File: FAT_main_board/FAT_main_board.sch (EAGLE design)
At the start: 19 parts, among them IC1 74LS241N

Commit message: [FAT board] Adds UART and I2C connectors.
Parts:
- added I2C0, I2C1, I2C2, UART1, UART2, UART3, UART4: (no value), con-lstb:MA04-1
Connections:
- removed net N$13: U$1.GND
- removed net RX0: U$1.0/RX
- removed net TX0: U$1.1/TX
- new net RX1: U$1.0/RX, UART1.1
- new net TX1: U$1.1/TX, UART1.2
- net GND: now also I2C0.3, I2C1.3, I2C2.3, U$1.GND, UART1.3, UART2.3, UART3.3, UART4.3
- net RX2: now also UART2.1
- net RX3: now also UART3.1
- net RX4: now also UART4.1
- net SCL0: now also I2C0.1
- net SCL1: now also I2C1.1
- net SCL2: now also I2C2.1
- net SDA0: now also I2C0.2
- net SDA1: now also I2C1.2
- net SDA2: now also I2C2.2
- net TX2: now also UART2.2
- net TX3: now also UART3.2
- net TX4: now also UART4.2
- net VCC: now also I2C0.4, I2C1.4, I2C2.4, U$1.VIN, UART1.4, UART2.4, UART3.4, UART4.4
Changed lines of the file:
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@@
 <part name="R4" library="resistor" deviceset="R-EU_" device="0204/7" value="10K"/>
 <part name="SV1" library="con-lstb" deviceset="MA03-1" device=""/>
+<part name="UART1" library="con-lstb" deviceset="MA04-1" device=""/>
+<part name="UART2" library="con-lstb" deviceset="MA04-1" device=""/>
+<part name="I2C0" library="con-lstb" deviceset="MA04-1" device=""/>
+<part name="I2C1" library="con-lstb" deviceset="MA04-1" device=""/>
+<part name="UART3" library="con-lstb" deviceset="MA04-1" device=""/>
+<part name="UART4" library="con-lstb" deviceset="MA04-1" device=""/>
+<part name="I2C2" library="con-lstb" deviceset="MA04-1" device=""/>
 </parts>
 <sheets>
@@
 <instance part="R4" gate="G$1" x="119.38" y="-99.06" rot="R90"/>
 <instance part="SV1" gate="G$1" x="213.36" y="-116.84" rot="R180"/>
+<instance part="UART1" gate="1" x="-111.76" y="25.4"/>
+<instance part="UART2" gate="1" x="-111.76" y="7.62"/>
+<instance part="I2C0" gate="1" x="-142.24" y="25.4"/>
+<instance part="I2C1" gate="1" x="-142.24" y="7.62"/>
+<instance part="UART3" gate="1" x="-111.76" y="-12.7"/>
+<instance part="UART4" gate="1" x="-111.76" y="-33.02"/>
+<instance part="I2C2" gate="1" x="-142.24" y="-12.7"/>
 </instances>
 <busses>
@@
 <label x="185.42" y="-114.3" size="1.778" layer="95"/>
 </segment>
+<segment>
+<pinref part="U$1" gate="G$1" pin="GND"/>
+<wire x1="-20.32" y1="22.86" x2="-27.94" y2="22.86" width="0.1524" layer="91"/>
+<label x="-27.94" y="22.86" size="1.778" layer="95"/>
+</segment>
+<segment>
+<pinref part="UART1" gate="1" pin="3"/>
+<wire x1="-104.14" y1="25.4" x2="-93.98" y2="25.4" width="0.1524" layer="91"/>
+<label x="-99.06" y="25.4" size="1.778" layer="95"/>
+</segment>
+<segment>
+<pinref part="UART2" gate="1" pin="3"/>
+<wire x1="-93.98" y1="7.62" x2="-104.14" y2="7.62" width="0.1524" layer="91"/>
+<label x="-99.06" y="7.62" size="1.778" layer="95"/>
+</segment>
+<segment>
+<pinref part="UART3" gate="1" pin="3"/>
+<wire x1="-93.98" y1="-12.7" x2="-104.14" y2="-12.7" width="0.1524" layer="91"/>
+<label x="-99.06" y="-12.7" size="1.778" layer="95"/>
+</segment>
+<segment>
+<pinref part="UART4" gate="1" pin="3"/>
+<wire x1="-93.98" y1="-33.02" x2="-104.14" y2="-33.02" width="0.1524" layer="91"/>
+<label x="-99.06" y="-33.02" size="1.778" layer="95"/>
+</segment>
+<segment>
+<pinref part="I2C0" gate="1" pin="3"/>
+<wire x1="-134.62" y1="25.4" x2="-124.46" y2="25.4" width="0.1524" layer="91"/>
+<label x="-129.54" y="25.4" size="1.778" layer="95"/>
+</segment>
+<segment>
+<pinref part="I2C1" gate="1" pin="3"/>
+<wire x1="-134.62" y1="7.62" x2="-124.46" y2="7.62" width="0.1524" layer="91"/>
+<label x="-129.54" y="7.62" size="1.778" layer="95"/>
+</segment>
+<segment>
+<pinref part="I2C2" gate="1" pin="3"/>
+<wire x1="-134.62" y1="-12.7" x2="-124.46" y2="-12.7" width="0.1524" layer="91"/>
+<label x="-129.54" y="-12.7" size="1.778" layer="95"/>
+</segment>
 </net>
 <net name="VCC" class="0">
@@
 <wire x1="109.22" y1="-124.46" x2="99.06" y2="-124.46" width="0.1524" layer="91"/>
 <label x="99.06" y="-124.46" size="1.778" layer="95"/>
+</segment>
+<segment>
+<pinref part="U$1" gate="G$1" pin="VIN"/>
+<wire x1="20.32" y1="22.86" x2="30.48" y2="22.86" width="0.1524" layer="91"/>
+<label x="25.4" y="22.86" size="1.778" layer="95"/>
+</segment>
+<segment>
+<pinref part="UART1" gate="1" pin="4"/>
+<wire x1="-104.14" y1="27.94" x2="-93.98" y2="27.94" width="0.1524" layer="91"/>
+<label x="-99.06" y="27.94" size="1.778" layer="95"/>
+</segment>
+<segment>
+<pinref part="UART2" gate="1" pin="4"/>
+<wire x1="-104.14" y1="10.16" x2="-93.98" y2="10.16" width="0.1524" layer="91"/>
+<label x="-99.06" y="10.16" size="1.778" layer="95"/>
+</segment>
+<segment>
+<pinref part="UART3" gate="1" pin="4"/>
+<wire x1="-104.14" y1="-10.16" x2="-93.98" y2="-10.16" width="0.1524" layer="91"/>
+<label x="-99.06" y="-10.16" size="1.778" layer="95"/>
+</segment>
+<segment>
+<pinref part="UART4" gate="1" pin="4"/>
+<wire x1="-104.14" y1="-30.48" x2="-93.98" y2="-30.48" width="0.1524" layer="91"/>
+<label x="-99.06" y="-30.48" size="1.778" layer="95"/>
+</segment>
+<segment>
+<pinref part="I2C0" gate="1" pin="4"/>
+<wire x1="-124.46" y1="27.94" x2="-134.62" y2="27.94" width="0.1524" layer="91"/>
+<label x="-129.54" y="27.94" size="1.778" layer="95"/>
+</segment>
+<segment>
+<pinref part="I2C1" gate="1" pin="4"/>
+<wire x1="-124.46" y1="10.16" x2="-134.62" y2="10.16" width="0.1524" layer="91"/>
+<label x="-129.54" y="10.16" size="1.778" layer="95"/>
+</segment>
+<segment>
+<pinref part="I2C2" gate="1" pin="4"/>
+<wire x1="-124.46" y1="-10.16" x2="-134.62" y2="-10.16" width="0.1524" layer="91"/>
+<label x="-129.54" y="-10.16" size="1.778" layer="95"/>
 </segment>
 </net>
@@
 <label x="25.4" y="5.08" size="1.778" layer="95"/>
 </segment>
+<segment>
+<pinref part="I2C0" gate="1" pin="1"/>
+<wire x1="-134.62" y1="20.32" x2="-124.46" y2="20.32" width="0.1524" layer="91"/>
+<label x="-129.54" y="20.32" size="1.778" layer="95"/>
+</segment>
 </net>
 <net name="SDA0" class="0">
@@
 <label x="25.4" y="2.54" size="1.778" layer="95"/>
 </segment>
+<segment>
+<pinref part="I2C0" gate="1" pin="2"/>
+<wire x1="-124.46" y1="22.86" x2="-134.62" y2="22.86" width="0.1524" layer="91"/>
+<label x="-129.54" y="22.86" size="1.778" layer="95"/>
+</segment>
 </net>
 <net name="SDA1" class="0">
@@
 <label x="25.4" y="-22.86" size="1.778" layer="95"/>
 </segment>
+<segment>
+<pinref part="I2C1" gate="1" pin="2"/>
+<wire x1="-124.46" y1="5.08" x2="-134.62" y2="5.08" width="0.1524" layer="91"/>
+<label x="-129.54" y="5.08" size="1.778" layer="95"/>
+</segment>
 </net>
 <net name="SCL1" class="0">
@@
 <label x="25.4" y="-25.4" size="1.778" layer="95"/>
 </segment>
+<segment>
+<pinref part="I2C1" gate="1" pin="1"/>
+<wire x1="-134.62" y1="2.54" x2="-124.46" y2="2.54" width="0.1524" layer="91"/>
+<label x="-129.54" y="2.54" size="1.778" layer="95"/>
+</segment>
 </net>
 <net name="RX5" class="0">
@@
 <label x="-30.48" y="-35.56" size="1.778" layer="95"/>
 </segment>
+<segment>
+<pinref part="UART4" gate="1" pin="2"/>
+<wire x1="-104.14" y1="-35.56" x2="-93.98" y2="-35.56" width="0.1524" layer="91"/>
+<label x="-99.06" y="-35.56" size="1.778" layer="95"/>
+</segment>
 </net>
 <net name="RX4" class="0">
@@
 <label x="-30.48" y="-33.02" size="1.778" layer="95"/>
 </segment>
+<segment>
+<pinref part="UART4" gate="1" pin="1"/>
+<wire x1="-93.98" y1="-38.1" x2="-104.14" y2="-38.1" width="0.1524" layer="91"/>
+<label x="-99.06" y="-38.1" size="1.778" layer="95"/>
+</segment>
 </net>
 <net name="N$40" class="0">
@@
 <label x="-30.48" y="-5.08" size="1.778" layer="95"/>
 </segment>
+<segment>
+<pinref part="UART2" gate="1" pin="2"/>
+<wire x1="-104.14" y1="5.08" x2="-93.98" y2="5.08" width="0.1524" layer="91"/>
+<label x="-99.06" y="5.08" size="1.778" layer="95"/>
+</segment>
 </net>
 <net name="RX2" class="0">
@@
 <label x="-30.48" y="-2.54" size="1.778" layer="95"/>
 </segment>
+<segment>
+<pinref part="UART2" gate="1" pin="1"/>
+<wire x1="-93.98" y1="2.54" x2="-104.14" y2="2.54" width="0.1524" layer="91"/>
+<label x="-99.06" y="2.54" size="1.778" layer="95"/>
+</segment>
 </net>
 <net name="TX3" class="0">
@@
 <label x="-30.48" y="0" size="1.778" layer="95"/>
 </segment>
+<segment>
+<pinref part="UART3" gate="1" pin="2"/>
+<wire x1="-104.14" y1="-15.24" x2="-93.98" y2="-15.24" width="0.1524" layer="91"/>
+<label x="-99.06" y="-15.24" size="1.778" layer="95"/>
+</segment>
 </net>
 <net name="RX3" class="0">
@@
 <label x="-30.48" y="2.54" size="1.778" layer="95"/>
 </segment>
-</net>
-<net name="RX0" class="0">
+<segment>
+<pinref part="UART3" gate="1" pin="1"/>
+<wire x1="-93.98" y1="-17.78" x2="-104.14" y2="-17.78" width="0.1524" layer="91"/>
+<label x="-99.06" y="-17.78" size="1.778" layer="95"/>
+</segment>
+</net>
+<net name="RX1" class="0">
 <segment>
 <pinref part="U$1" gate="G$1" pin="0/RX"/>
@@
 <label x="-30.48" y="20.32" size="1.778" layer="95"/>
 </segment>
-</net>
-<net name="TX0" class="0">
+<segment>
+<pinref part="UART1" gate="1" pin="1"/>
+<wire x1="-104.14" y1="20.32" x2="-93.98" y2="20.32" width="0.1524" layer="91"/>
+<label x="-99.06" y="20.32" size="1.778" layer="95"/>
+</segment>
+</net>
+<net name="TX1" class="0">
 <segment>
 <pinref part="U$1" gate="G$1" pin="1/TX"/>
@@
 <label x="-30.48" y="17.78" size="1.778" layer="95"/>
 </segment>
+<segment>
+<pinref part="UART1" gate="1" pin="2"/>
+<wire x1="-93.98" y1="22.86" x2="-104.14" y2="22.86" width="0.1524" layer="91"/>
+<label x="-99.06" y="22.86" size="1.778" layer="95"/>
+</segment>
 </net>
 <net name="SCL2" class="0">
@@
 <label x="-30.48" y="12.7" size="1.778" layer="95"/>
 </segment>
+<segment>
+<pinref part="I2C2" gate="1" pin="1"/>
+<wire x1="-134.62" y1="-17.78" x2="-124.46" y2="-17.78" width="0.1524" layer="91"/>
+<label x="-129.54" y="-17.78" size="1.778" layer="95"/>
+</segment>
 </net>
 <net name="SDA2" class="0">
@@
 <label x="-30.48" y="10.16" size="1.778" layer="95"/>
 </segment>
+<segment>
+<pinref part="I2C2" gate="1" pin="2"/>
+<wire x1="-124.46" y1="-15.24" x2="-134.62" y2="-15.24" width="0.1524" layer="91"/>
+<label x="-129.54" y="-15.24" size="1.778" layer="95"/>
+</segment>
 </net>
 <net name="N$9" class="0">
@@
 </segment>
 </net>
-<net name="N$13" class="0">
-<segment>
-<pinref part="U$1" gate="G$1" pin="GND"/>
-<wire x1="-20.32" y1="22.86" x2="-27.94" y2="22.86" width="0.1524" layer="91"/>
-</segment>
-</net>

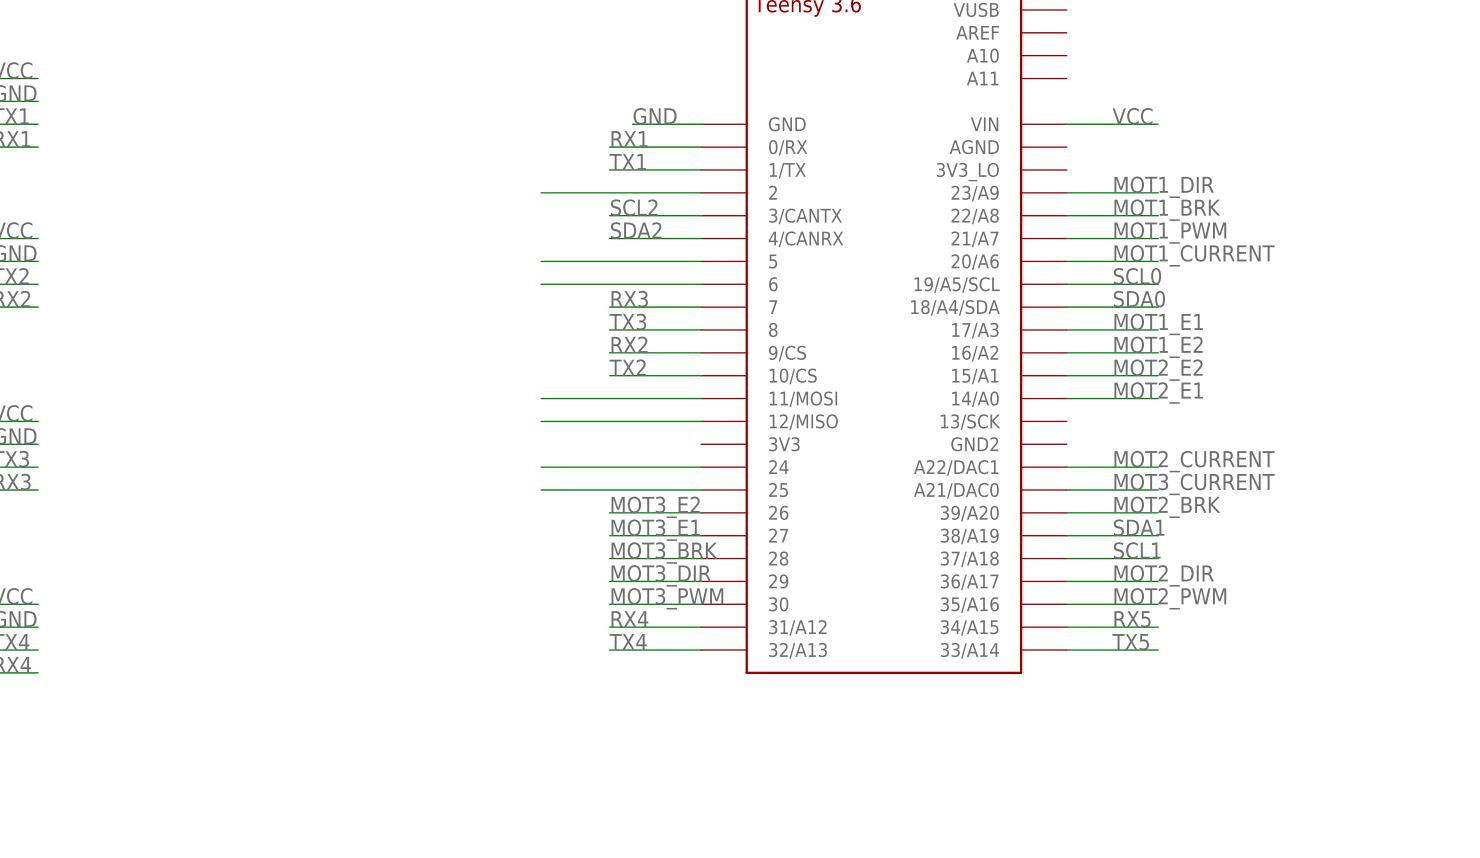
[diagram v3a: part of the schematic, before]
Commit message: [FAT board] Adds connector for free pins.
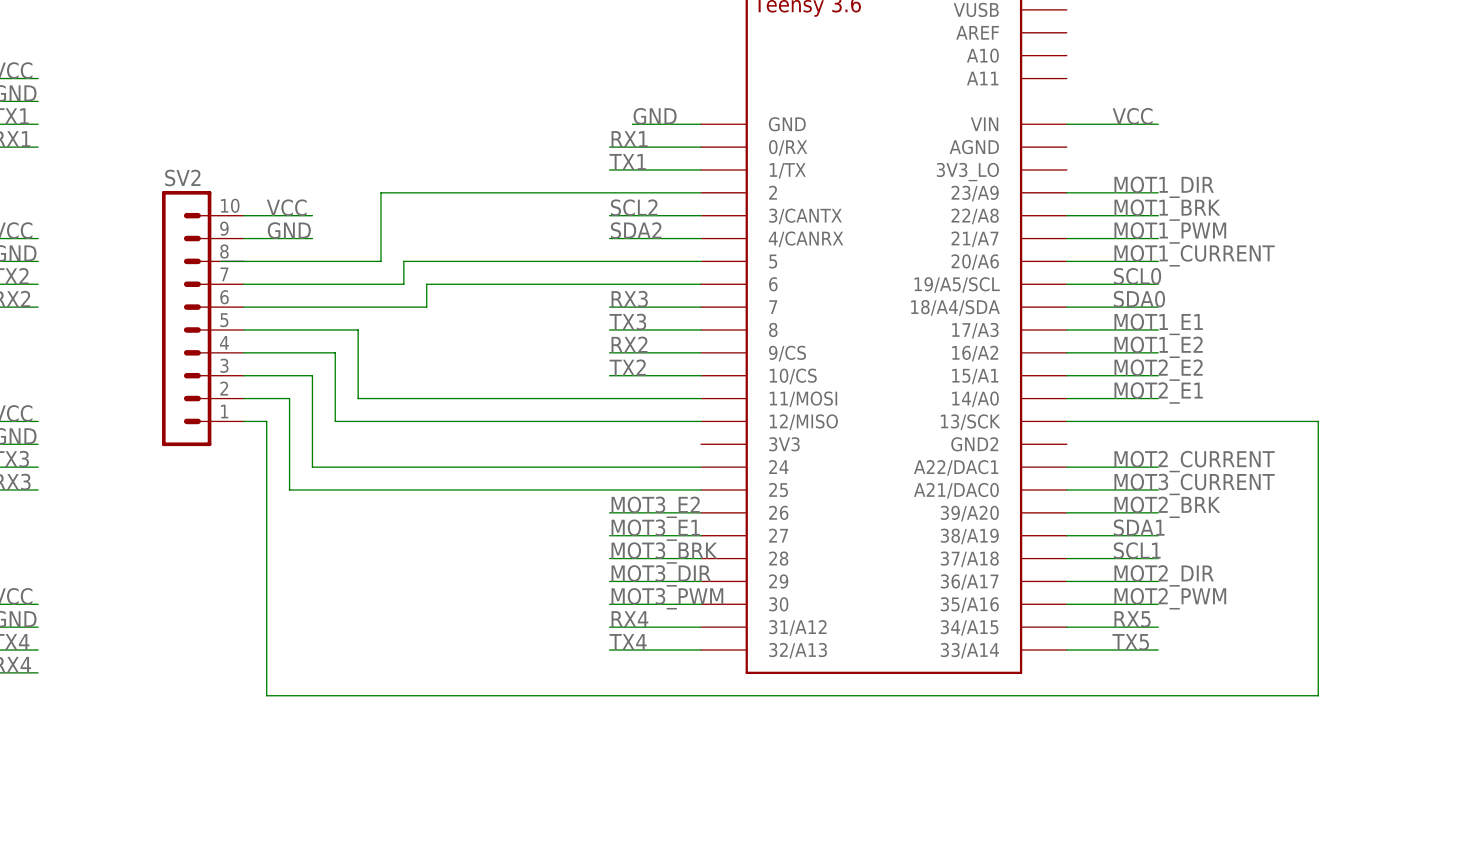
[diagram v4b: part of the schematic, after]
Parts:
- added SV2: (no value), con-lstb:MA10-1
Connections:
- new net N$24: SV2.1, U$1.13/SCK
- net GND: now also SV2.9
- net N$10: now also SV2.6
- net N$11: now also SV2.5
- net N$12: now also SV2.4
- net N$40: now also SV2.2
- net N$41: now also SV2.3
- net N$9: now also SV2.7
- net VCC: now also SV2.10
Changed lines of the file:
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@@
 <part name="UART4" library="con-lstb" deviceset="MA04-1" device=""/>
 <part name="I2C2" library="con-lstb" deviceset="MA04-1" device=""/>
+<part name="SV2" library="con-lstb" deviceset="MA10-1" device=""/>
 </parts>
 <sheets>
@@
 <instance part="UART4" gate="1" x="-111.76" y="-33.02"/>
 <instance part="I2C2" gate="1" x="-142.24" y="-12.7"/>
+<instance part="SV2" gate="1" x="-78.74" y="0"/>
 </instances>
 <busses>
@@
 <label x="-129.54" y="-12.7" size="1.778" layer="95"/>
 </segment>
+<segment>
+<pinref part="SV2" gate="1" pin="9"/>
+<wire x1="-71.12" y1="10.16" x2="-63.5" y2="10.16" width="0.1524" layer="91"/>
+<label x="-68.58" y="10.16" size="1.778" layer="95"/>
+</segment>
 </net>
 <net name="VCC" class="0">
@@
 <wire x1="-124.46" y1="-10.16" x2="-134.62" y2="-10.16" width="0.1524" layer="91"/>
 <label x="-129.54" y="-10.16" size="1.778" layer="95"/>
+</segment>
+<segment>
+<pinref part="SV2" gate="1" pin="10"/>
+<wire x1="-71.12" y1="12.7" x2="-63.5" y2="12.7" width="0.1524" layer="91"/>
+<label x="-68.58" y="12.7" size="1.778" layer="95"/>
 </segment>
 </net>
@@
 <segment>
 <pinref part="U$1" gate="G$1" pin="25"/>
-<wire x1="-38.1" y1="-17.78" x2="-20.32" y2="-17.78" width="0.1524" layer="91"/>
+<pinref part="SV2" gate="1" pin="2"/>
+<wire x1="-71.12" y1="-7.62" x2="-66.04" y2="-7.62" width="0.1524" layer="91"/>
+<wire x1="-66.04" y1="-7.62" x2="-66.04" y2="-17.78" width="0.1524" layer="91"/>
+<wire x1="-66.04" y1="-17.78" x2="-20.32" y2="-17.78" width="0.1524" layer="91"/>
 </segment>
 </net>
@@
 <segment>
 <pinref part="U$1" gate="G$1" pin="24"/>
-<wire x1="-20.32" y1="-15.24" x2="-38.1" y2="-15.24" width="0.1524" layer="91"/>
+<pinref part="SV2" gate="1" pin="3"/>
+<wire x1="-71.12" y1="-5.08" x2="-63.5" y2="-5.08" width="0.1524" layer="91"/>
+<wire x1="-63.5" y1="-5.08" x2="-63.5" y2="-15.24" width="0.1524" layer="91"/>
+<wire x1="-63.5" y1="-15.24" x2="-20.32" y2="-15.24" width="0.1524" layer="91"/>
 </segment>
 </net>
@@
 <segment>
 <pinref part="U$1" gate="G$1" pin="5"/>
-<wire x1="-20.32" y1="7.62" x2="-38.1" y2="7.62" width="0.1524" layer="91"/>
+<wire x1="-20.32" y1="7.62" x2="-53.34" y2="7.62" width="0.1524" layer="91"/>
+<pinref part="SV2" gate="1" pin="7"/>
+<wire x1="-71.12" y1="5.08" x2="-53.34" y2="5.08" width="0.1524" layer="91"/>
+<wire x1="-53.34" y1="5.08" x2="-53.34" y2="7.62" width="0.1524" layer="91"/>
 </segment>
 </net>
@@
 <segment>
 <pinref part="U$1" gate="G$1" pin="6"/>
-<wire x1="-38.1" y1="5.08" x2="-20.32" y2="5.08" width="0.1524" layer="91"/>
+<wire x1="-50.8" y1="5.08" x2="-20.32" y2="5.08" width="0.1524" layer="91"/>
+<pinref part="SV2" gate="1" pin="6"/>
+<wire x1="-71.12" y1="2.54" x2="-50.8" y2="2.54" width="0.1524" layer="91"/>
+<wire x1="-50.8" y1="2.54" x2="-50.8" y2="5.08" width="0.1524" layer="91"/>
 </segment>
 </net>
@@
 <segment>
 <pinref part="U$1" gate="G$1" pin="11/MOSI"/>
-<wire x1="-20.32" y1="-7.62" x2="-38.1" y2="-7.62" width="0.1524" layer="91"/>
+<pinref part="SV2" gate="1" pin="5"/>
+<wire x1="-71.12" y1="0" x2="-58.42" y2="0" width="0.1524" layer="91"/>
+<wire x1="-58.42" y1="0" x2="-58.42" y2="-7.62" width="0.1524" layer="91"/>
+<wire x1="-58.42" y1="-7.62" x2="-20.32" y2="-7.62" width="0.1524" layer="91"/>
 </segment>
 </net>
@@
 <segment>
 <pinref part="U$1" gate="G$1" pin="12/MISO"/>
-<wire x1="-38.1" y1="-10.16" x2="-20.32" y2="-10.16" width="0.1524" layer="91"/>
+<pinref part="SV2" gate="1" pin="4"/>
+<wire x1="-71.12" y1="-2.54" x2="-60.96" y2="-2.54" width="0.1524" layer="91"/>
+<wire x1="-60.96" y1="-2.54" x2="-60.96" y2="-10.16" width="0.1524" layer="91"/>
+<wire x1="-60.96" y1="-10.16" x2="-20.32" y2="-10.16" width="0.1524" layer="91"/>
 </segment>
 </net>
@@
 <segment>
 <pinref part="U$1" gate="G$1" pin="2"/>
-<wire x1="-20.32" y1="15.24" x2="-38.1" y2="15.24" width="0.1524" layer="91"/>
+<wire x1="-73.66" y1="7.62" x2="-55.88" y2="7.62" width="0.1524" layer="91"/>
+<wire x1="-55.88" y1="7.62" x2="-55.88" y2="15.24" width="0.1524" layer="91"/>
+<wire x1="-55.88" y1="15.24" x2="-20.32" y2="15.24" width="0.1524" layer="91"/>
 </segment>
 </net>
@@
 </segment>
 </net>
+<net name="N$24" class="0">
+<segment>
+<pinref part="U$1" gate="G$1" pin="13/SCK"/>
+<wire x1="20.32" y1="-10.16" x2="48.26" y2="-10.16" width="0.1524" layer="91"/>
+<wire x1="48.26" y1="-10.16" x2="48.26" y2="-40.64" width="0.1524" layer="91"/>
+<wire x1="48.26" y1="-40.64" x2="-68.58" y2="-40.64" width="0.1524" layer="91"/>
+<wire x1="-68.58" y1="-40.64" x2="-68.58" y2="-10.16" width="0.1524" layer="91"/>
+<pinref part="SV2" gate="1" pin="1"/>
+<wire x1="-68.58" y1="-10.16" x2="-71.12" y2="-10.16" width="0.1524" layer="91"/>
+</segment>
+</net>
